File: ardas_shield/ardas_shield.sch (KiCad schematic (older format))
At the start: 37 parts, among them CON1 SD_Card, IC1 DS1307, P1 CONN_10, P10 CONN_01X03, P2 CONN_8, P3 CONN_8, P4 CONN_ICSP, P5 CONN_6, P6 TTL_COMM, P7 CONN_01X03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

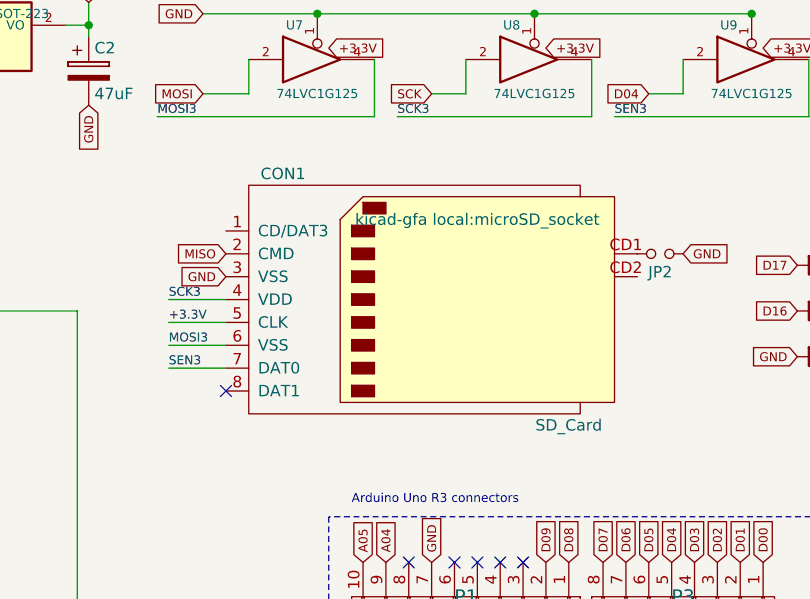
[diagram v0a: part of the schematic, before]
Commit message: removing CON1 SD card
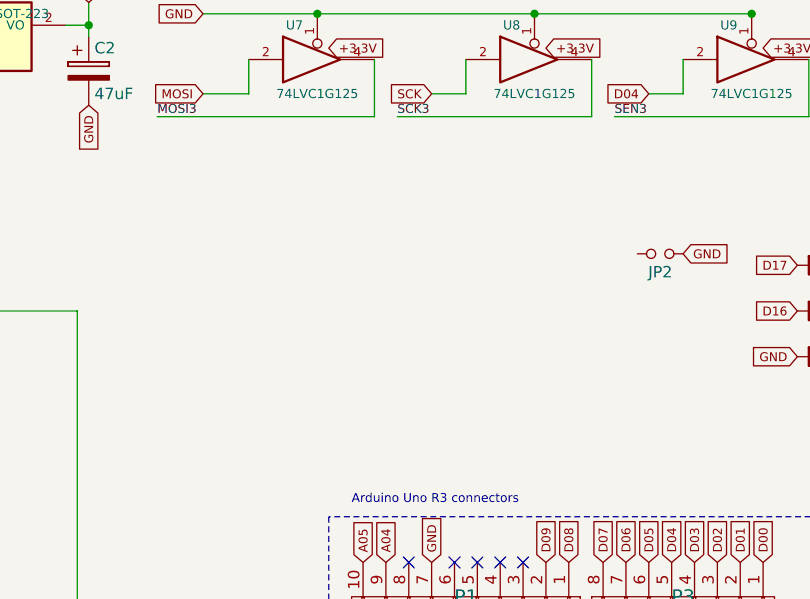
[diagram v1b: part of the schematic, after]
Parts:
- removed CON1: SD_Card, kicad-gfa local:microSD_socket, symbol SD_Card
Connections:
- no-connect marks 20 -> 19
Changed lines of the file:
@@
 Text GLabel 10600 1250 0    39   Input ~ 0
 SCK
-Text GLabel 9700 1950 0    39   Input ~ 0
-MISO
-Text GLabel 9700 2050 0    39   Input ~ 0
-GND
-Text Label 9450 2150 0    39   ~ 0
-SCK3
-Text Label 9450 2250 0    39   ~ 0
-+3.3V
 Text GLabel 8600 1250 3    39   Input ~ 0
 GND
-Text Label 9450 2350 0    39   ~ 0
-MOSI3
-Text Label 9450 2450 0    39   ~ 0
-SEN3
 $Comp
 L CONN_02X03 P4
@@
 Text GLabel 12050 4150 2    39   Input ~ 0
 GND
-NoConn ~ 9700 2550
 Text Notes 12850 3050 0    39   ~ 0
 Rx
@@
 NoConn ~ 2000 4200
 NoConn ~ 13200 1000
-$Comp
-L SD_Card CON1
-U 1 1 5655FE06
-P 10600 2150
-F 0 "CON1" H 9950 2700 50  0000 C CNN
-F 1 "SD_Card" H 11200 1600 50  0000 C CNN
-F 2 "kicad-gfa local:microSD_socket" H 10800 2500 50  0000 C CNN
-F 3 "https://github.com/UMONS-GFA/kicad-gfa.pretty/blob/master/datasheets/1717993.pdf" H 10600 2150 60  0001 C CNN
-F 4 "2334075" H 10600 2150 60  0001 C CNN "Order_Code"
-F 5 "MOLEX" H 10600 2150 60  0001 C CNN "MFN"
-F 6 "503182-1853" H 10600 2150 60  0001 C CNN "MFP"
-	1    10600 2150
-	1    0    0    -1
-$EndComp
 Wire Wire Line
 	5300 1600 5300 2600
@@
 Wire Notes Line
 	12300 5000 12300 3100
-Wire Wire Line
-	9700 2150 9450 2150
-Wire Wire Line
-	9700 2250 9450 2250
 Wire Wire Line
 	11700 1250 11550 1250
@@
 Text GLabel 11700 1950 2    39   Input ~ 0
 GND
-Wire Wire Line
-	9700 2350 9450 2350
-Wire Wire Line
-	9700 2450 9450 2450
 Text GLabel 10150 1050 2    39   Input ~ 0
 +3.3V

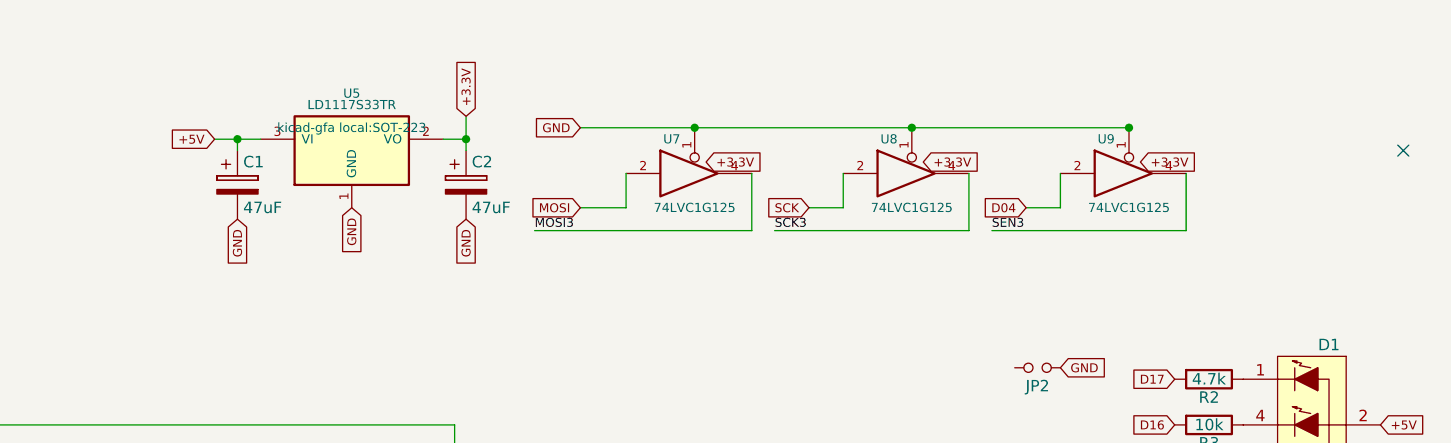
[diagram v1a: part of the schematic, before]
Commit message: removing 5V-3.3V converter components from scheme
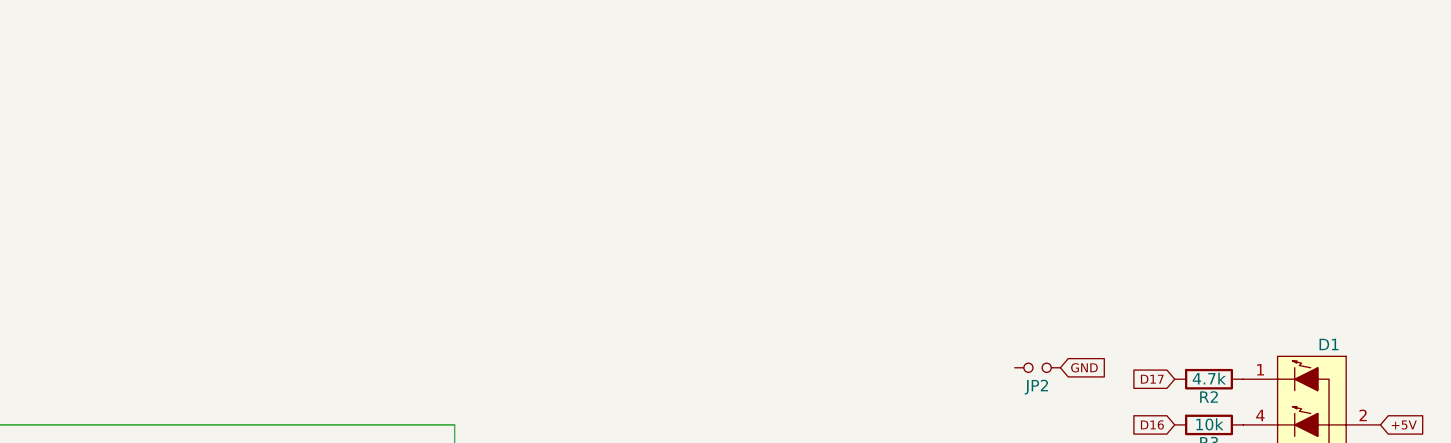
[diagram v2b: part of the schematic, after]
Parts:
- removed C1, C2: 47uF, kicad-gfa local:C_0805, symbol CP
- removed U5: LD1117S33TR, kicad-gfa local:SOT-223, symbol LD1117S33TR
- removed U7, U8, U9: 74LVC1G125, kicad-gfa local:SC-70-5, symbol 74LVC1G125
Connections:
- no-connect marks 19 -> 18
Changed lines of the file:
@@
 	1    0    0    -1
 $EndComp
-Text GLabel 9100 1300 3    39   Input ~ 0
-GND
 Text Notes 10250 3050 0    39   ~ 0
 Arduino Uno R3 connectors
-Text GLabel 8100 1300 3    39   Input ~ 0
-GND
-Text GLabel 9600 900  0    39   Input ~ 0
-GND
-$Comp
-L 74LVC1G125 U7
-U 1 1 56550034
-P 10100 1100
-F 0 "U7" H 10000 1250 40  0000 C CNN
-F 1 "74LVC1G125" H 10100 950 40  0000 C CNN
-F 2 "kicad-gfa local:SC-70-5" H 10100 1100 60  0001 C CNN
-F 3 "" H 10100 1100 60  0000 C CNN
-	1    10100 1100
-	1    0    0    -1
-$EndComp
-$Comp
-L 74LVC1G125 U8
-U 1 1 56550392
-P 11050 1100
-F 0 "U8" H 10950 1250 40  0000 C CNN
-F 1 "74LVC1G125" H 11050 950 40  0000 C CNN
-F 2 "kicad-gfa local:SC-70-5" H 11050 1100 60  0001 C CNN
-F 3 "" H 11050 1100 60  0000 C CNN
-	1    11050 1100
-	1    0    0    -1
-$EndComp
-$Comp
-L 74LVC1G125 U9
-U 1 1 5655048F
-P 12000 1100
-F 0 "U9" H 11900 1250 40  0000 C CNN
-F 1 "74LVC1G125" H 12000 950 40  0000 C CNN
-F 2 "kicad-gfa local:SC-70-5" H 12000 1100 60  0001 C CNN
-F 3 "" H 12000 1100 60  0000 C CNN
-	1    12000 1100
-	1    0    0    -1
-$EndComp
-Text Label 9400 1350 0    39   ~ 0
-MOSI3
-Text Label 10450 1350 0    39   ~ 0
-SCK3
-Text Label 11400 1350 0    39   ~ 0
-SEN3
-Text GLabel 11550 1250 0    39   Input ~ 0
-D04
-$Comp
-L LD1117S33TR U5
-U 1 1 565533AB
-P 8600 1000
-F 0 "U5" H 8600 1250 40  0000 C CNN
-F 1 "LD1117S33TR" H 8600 1200 40  0000 C CNN
-F 2 "kicad-gfa local:SOT-223" H 8600 1100 40  0000 C CNN
-F 3 "https://github.com/UMONS-GFA/kicad-gfa.pretty/blob/master/datasheets/1776449.pdf" H 8600 1000 60  0001 C CNN
-F 4 "1202826" H 8600 1000 60  0001 C CNN "Order_Code"
-F 5 "STMICROELECTRONICS" H 8600 1000 60  0001 C CNN "MFN"
-F 6 " LD1117S33TR" H 8600 1000 60  0001 C CNN "MFP"
-	1    8600 1000
-	1    0    0    -1
-$EndComp
-$Comp
-L CP C1
-U 1 1 565535F2
-P 8100 1150
-F 0 "C1" H 8125 1250 50  0000 L CNN
-F 1 "47uF" H 8125 1050 50  0000 L CNN
-F 2 "kicad-gfa local:C_0805" H 8138 1000 30  0001 C CNN
-F 3 "" H 8100 1150 60  0000 C CNN
-	1    8100 1150
-	1    0    0    -1
-$EndComp
-$Comp
-L CP C2
-U 1 1 565536BD
-P 9100 1150
-F 0 "C2" H 9125 1250 50  0000 L CNN
-F 1 "47uF" H 9125 1050 50  0000 L CNN
-F 2 "kicad-gfa local:C_0805" H 9138 1000 30  0001 C CNN
-F 3 "" H 9100 1150 60  0000 C CNN
-	1    9100 1150
-	1    0    0    -1
-$EndComp
-Text GLabel 8000 950  0    39   Input ~ 0
-+5V
-Text GLabel 9600 1250 0    39   Input ~ 0
-MOSI
-Text GLabel 10600 1250 0    39   Input ~ 0
-SCK
-Text GLabel 8600 1250 3    39   Input ~ 0
-GND
 $Comp
 L CONN_02X03 P4
@@
 	1    0    0    -1
 $EndComp
-Text GLabel 11100 1050 2    39   Input ~ 0
-+3.3V
-Text GLabel 12050 1050 2    39   Input ~ 0
-+3.3V
 $Comp
 L Battery BT1
@@
 NoConn ~ 4600 2100
 NoConn ~ 2000 4200
-NoConn ~ 13200 1000
 Wire Wire Line
 	5300 1600 5300 2600
@@
 Wire Notes Line
 	12300 5000 12300 3100
-Wire Wire Line
-	11700 1250 11550 1250
-Wire Wire Line
-	10750 1250 10600 1250
-Wire Wire Line
-	9800 1250 9600 1250
-Connection ~ 8100 950
-Wire Wire Line
-	8000 950  8200 950
-Wire Wire Line
-	8100 1000 8100 950
-Connection ~ 9100 950
-Wire Wire Line
-	9100 850  9100 1000
-Wire Wire Line
-	9000 950  9100 950
-Wire Wire Line
-	10350 1350 10350 1100
-Wire Wire Line
-	9400 1350 10350 1350
-Wire Wire Line
-	9800 1100 9800 1250
-Wire Wire Line
-	12250 1350 12250 1100
-Wire Wire Line
-	11400 1350 12250 1350
-Wire Wire Line
-	11700 1100 11700 1250
-Wire Wire Line
-	11300 1350 10450 1350
-Wire Wire Line
-	11300 1100 11300 1350
-Wire Wire Line
-	10750 1100 10750 1250
-Connection ~ 11050 900
-Connection ~ 10100 900
 Wire Notes Line
 	10150 3100 10150 5000
@@
 Connection ~ 6950 4300
 Connection ~ 6950 4000
-Connection ~ 12000 900
-Wire Wire Line
-	9600 900  12000 900
 Wire Wire Line
 	6950 4000 6950 4300
@@
 Text GLabel 11700 1950 2    39   Input ~ 0
 GND
-Text GLabel 10150 1050 2    39   Input ~ 0
-+3.3V
-Text GLabel 9100 850  1    39   Input ~ 0
-+3.3V
 Text Notes 9250 6650 0    60   Italic 12
 SHOULDN'T WE SET PIN 10 TO GND OR VCC?

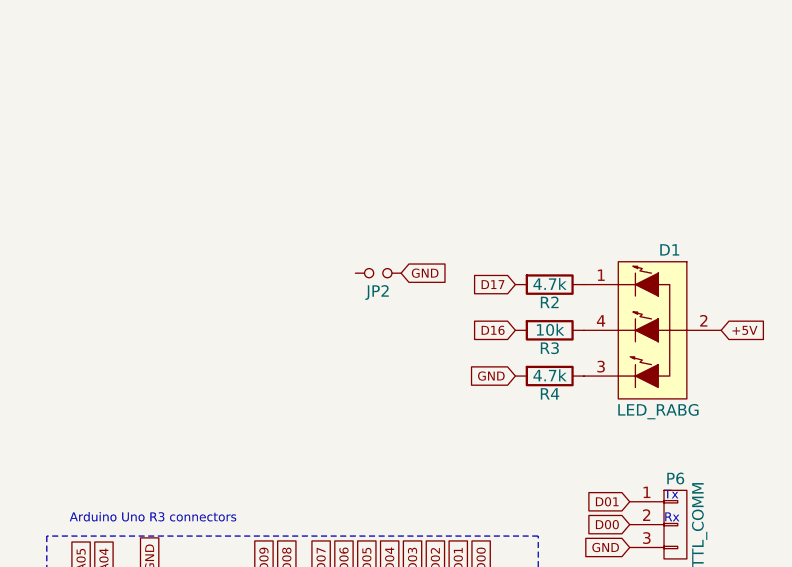
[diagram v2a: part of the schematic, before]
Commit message: removing JP2 from scheme
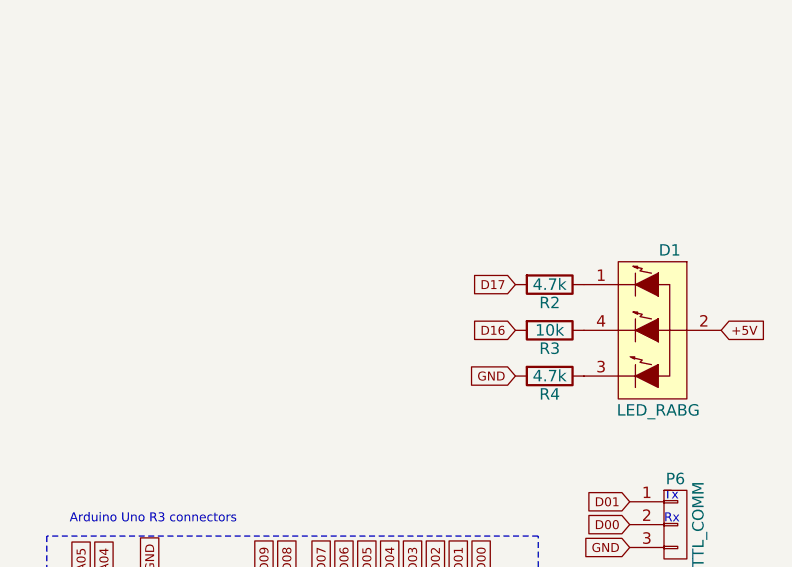
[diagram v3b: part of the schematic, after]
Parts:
- removed JP2: Jumper_NO_Small, kicad-gfa local:small_no_jumper, symbol Jumper_NO_Small
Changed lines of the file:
@@
 NoConn ~ 11950 4800
 NoConn ~ 12050 4800
-$Comp
-L Jumper_NO_Small JP2
-U 1 1 569E9D5A
-P 11600 1950
-F 0 "JP2" H 11600 2030 50  0000 C CNN
-F 1 "Jumper_NO_Small" H 11610 1890 50  0001 C CNN
-F 2 "kicad-gfa local:small_no_jumper" H 11600 1950 50  0001 C CNN
-F 3 "" H 11600 1950 50  0000 C CNN
-	1    11600 1950
-	-1   0    0    1
-$EndComp
-Text GLabel 11700 1950 2    39   Input ~ 0
-GND
 Text Notes 9250 6650 0    60   Italic 12
 SHOULDN'T WE SET PIN 10 TO GND OR VCC?

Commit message: resolve rules check problems
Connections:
- net D04: no longer names the net of P3.5 (P5)
- net MISO: no longer names the net of P4.1 (P1)
- net MOSI: no longer names the net of P4.4 (P4)
- net SCK: no longer names the net of P4.3 (P3)
- no-connect marks 18 -> 22
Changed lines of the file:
@@
 Text GLabel 11750 3300 1    39   Input ~ 0
 D03
-Text GLabel 11650 3300 1    39   Input ~ 0
-D04
 Text GLabel 11550 3300 1    39   Input ~ 0
 D05
@@
 Text GLabel 12050 3950 2    39   Input ~ 0
 +5V
-Text GLabel 11550 3950 0    39   Input ~ 0
-MISO
-Text GLabel 11550 4050 0    39   Input ~ 0
-SCK
-Text GLabel 12050 4050 2    39   Input ~ 0
-MOSI
 Text GLabel 12050 4150 2    39   Input ~ 0
 GND
@@
 Text Notes 9250 6650 0    60   Italic 12
 SHOULDN'T WE SET PIN 10 TO GND OR VCC?
+NoConn ~ 12050 4050
+NoConn ~ 11550 3950
+NoConn ~ 11550 4050
+NoConn ~ 11650 3300
 $EndSCHEMATC

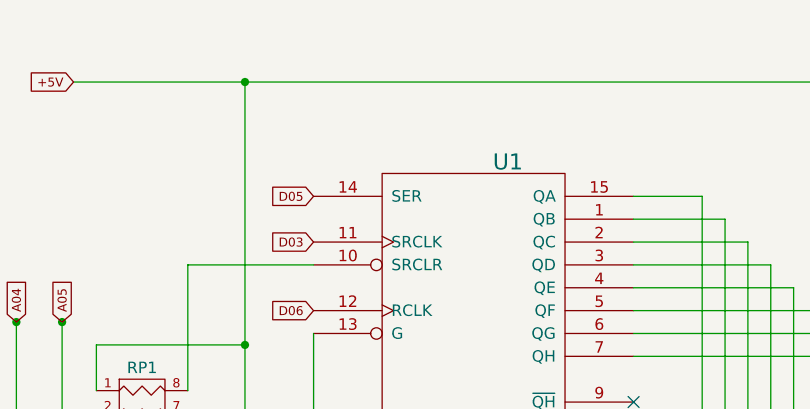
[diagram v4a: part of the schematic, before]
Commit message: resolve power input problem on U1
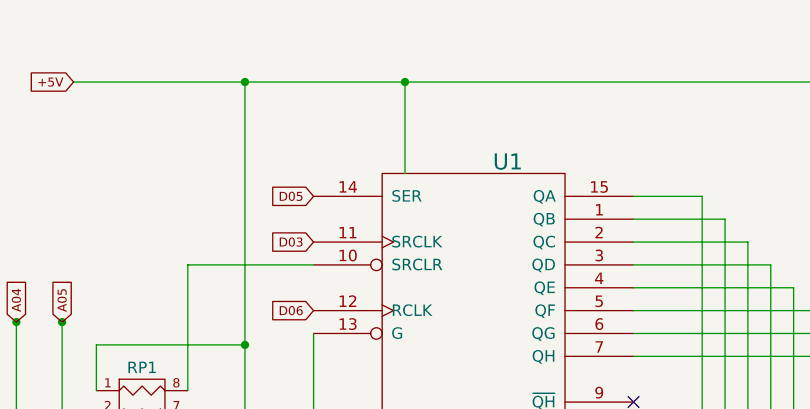
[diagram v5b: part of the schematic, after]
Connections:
- net VCC is gone; now on net +5V: U1.16 (VCC)
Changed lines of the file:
@@
 NoConn ~ 11550 4050
 NoConn ~ 11650 3300
+Wire Wire Line
+	3600 1100 3600 700
+Connection ~ 3600 700
 $EndSCHEMATC

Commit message: replace RGB Led circuit by separated leds
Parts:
- removed D1: LED_RABG, kicad-gfa local:led-P-LCC-4-3, symbol LED_RABG
- added D1, D2, D3: LED, symbol LED
- R2: value 4.7k -> R; footprint kicad-gfa local:R_0805 -> (none); Case_Style 0805 [2012 Metric] -> (none); MFN YAGEO (PHYCOMP) -> (none); MFP RC0805JR-07150RL -> (none); Order_Code 9233903RL -> (none)
- R3: value 10k -> R; footprint kicad-gfa local:R_0805 -> (none); Case_Style 0805 [2012 Metric] -> (none); MFN YAGEO (PHYCOMP) -> (none); MFP RC0805JR-07100RL -> (none); Order_Code 9233881 -> (none)
- R4: value 4.7k -> R; footprint kicad-gfa local:R_0805 -> (none); Case_Style 805 [2012 Metric] -> (none); MFN YAGEO (PHYCOMP) -> (none); MFP RC0805JR-07100RL -> (none); Order_Code 9233881 -> (none)
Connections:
- wire segments 194 -> 202
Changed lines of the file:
@@
 	-1   0    0    1
 $EndComp
-Text GLabel 12200 2200 0    39   Input ~ 0
+Text GLabel 10550 2250 0    39   Input ~ 0
 D16
 Text GLabel 11850 4800 3    39   Input ~ 0
 D17
-Text GLabel 12200 2000 0    39   Input ~ 0
+Text GLabel 10550 1950 0    39   Input ~ 0
 D17
 $Comp
@@
 	1    0    0    -1
 $EndComp
-$Comp
-L LED_RABG D1
-U 1 1 565885AB
-P 12800 2200
-F 0 "D1" H 12875 2550 50  0000 C CNN
-F 1 "LED_RABG" H 12825 1850 50  0000 C CNN
-F 2 "kicad-gfa local:led-P-LCC-4-3" H 12750 2150 50  0001 C CNN
-F 3 "https://github.com/UMONS-GFA/kicad-gfa.pretty/blob/master/datasheets/AV02-4186EN_DS_ASMB-MTB0_2014-09-10.pdf" H 12750 2150 50  0001 C CNN
-	1    12800 2200
-	1    0    0    -1
-$EndComp
-Text GLabel 13100 2200 2    39   Input ~ 0
+Text GLabel 11750 2250 2    39   Input ~ 0
 +5V
 NoConn ~ 10700 3300
-Text GLabel 12200 2400 0    39   Input ~ 0
+Text GLabel 10550 2550 0    39   Input ~ 0
 GND
 $Comp
@@
 Wire Wire Line
 	6500 5800 6500 5950
-$Comp
-L R R2
-U 1 1 568BE18A
-P 12350 2000
-F 0 "R2" V 12430 2000 50  0000 C CNN
-F 1 "4.7k" V 12350 2000 50  0000 C CNN
-F 2 "kicad-gfa local:R_0805" V 12280 2000 50  0001 C CNN
-F 3 "" H 12350 2000 50  0000 C CNN
-F 4 "9233903RL " V 12350 2000 60  0001 C CNN "Order_Code"
-F 5 "YAGEO (PHYCOMP) " V 12350 2000 60  0001 C CNN "MFN"
-F 6 "RC0805JR-07150RL" V 12350 2000 60  0001 C CNN "MFP"
-F 7 "0805 [2012 Metric]" V 12350 2000 60  0001 C CNN "Case_Style"
-	1    12350 2000
-	0    1    1    0
-$EndComp
-$Comp
-L R R3
-U 1 1 568BE39C
-P 12350 2200
-F 0 "R3" V 12430 2200 50  0000 C CNN
-F 1 "10k" V 12350 2200 50  0000 C CNN
-F 2 "kicad-gfa local:R_0805" V 12280 2200 50  0001 C CNN
-F 3 "" H 12350 2200 50  0000 C CNN
-F 4 "9233881" V 12350 2200 60  0001 C CNN "Order_Code"
-F 5 "YAGEO (PHYCOMP) " V 12350 2200 60  0001 C CNN "MFN"
-F 6 "RC0805JR-07100RL" V 12350 2200 60  0001 C CNN "MFP"
-F 7 "0805 [2012 Metric]" V 12350 2200 60  0001 C CNN "Case_Style"
-	1    12350 2200
-	0    1    1    0
-$EndComp
-$Comp
-L R R4
-U 1 1 568BE4E9
-P 12350 2400
-F 0 "R4" V 12430 2400 50  0000 C CNN
-F 1 "4.7k" V 12350 2400 50  0000 C CNN
-F 2 "kicad-gfa local:R_0805" V 12280 2400 50  0001 C CNN
-F 3 "" H 12350 2400 50  0000 C CNN
-F 4 "9233881" V 12350 2400 60  0001 C CNN "Order_Code"
-F 5 "YAGEO (PHYCOMP)" V 12350 2400 60  0001 C CNN "MFN"
-F 6 "RC0805JR-07100RL" V 12350 2400 60  0001 C CNN "MFP"
-F 7 "805 [2012 Metric]" V 12350 2400 60  0001 C CNN "Case_Style"
-	1    12350 2400
-	0    1    1    0
-$EndComp
 $Comp
 L Jumper_NO_Small JP1
@@
 	3600 1100 3600 700
 Connection ~ 3600 700
+$Comp
+L R R2
+U 1 1 5B0E7B52
+P 10800 1950
+F 0 "R2" V 10880 1950 50  0000 C CNN
+F 1 "R" V 10800 1950 50  0000 C CNN
+F 2 "" V 10730 1950 50  0000 C CNN
+F 3 "" H 10800 1950 50  0000 C CNN
+	1    10800 1950
+	0    1    1    0
+$EndComp
+$Comp
+L R R3
+U 1 1 5B0E7BC5
+P 10800 2250
+F 0 "R3" V 10880 2250 50  0000 C CNN
+F 1 "R" V 10800 2250 50  0000 C CNN
+F 2 "" V 10730 2250 50  0000 C CNN
+F 3 "" H 10800 2250 50  0000 C CNN
+	1    10800 2250
+	0    1    1    0
+$EndComp
+$Comp
+L R R4
+U 1 1 5B0E7C5F
+P 10800 2550
+F 0 "R4" V 10880 2550 50  0000 C CNN
+F 1 "R" V 10800 2550 50  0000 C CNN
+F 2 "" V 10730 2550 50  0000 C CNN
+F 3 "" H 10800 2550 50  0000 C CNN
+	1    10800 2550
+	0    1    1    0
+$EndComp
+$Comp
+L LED D1
+U 1 1 5B0E7D8D
+P 11300 1950
+F 0 "D1" H 11300 2050 50  0000 C CNN
+F 1 "LED" H 11300 1850 50  0000 C CNN
+F 2 "" H 11300 1950 50  0000 C CNN
+F 3 "" H 11300 1950 50  0000 C CNN
+	1    11300 1950
+	1    0    0    -1
+$EndComp
+$Comp
+L LED D2
+U 1 1 5B0E7E09
+P 11300 2250
+F 0 "D2" H 11300 2350 50  0000 C CNN
+F 1 "LED" H 11300 2150 50  0000 C CNN
+F 2 "" H 11300 2250 50  0000 C CNN
+F 3 "" H 11300 2250 50  0000 C CNN
+	1    11300 2250
+	1    0    0    -1
+$EndComp
+$Comp
+L LED D3
+U 1 1 5B0E7E8F
+P 11300 2550
+F 0 "D3" H 11300 2650 50  0000 C CNN
+F 1 "LED" H 11300 2450 50  0000 C CNN
+F 2 "" H 11300 2550 50  0000 C CNN
+F 3 "" H 11300 2550 50  0000 C CNN
+	1    11300 2550
+	1    0    0    -1
+$EndComp
+Wire Wire Line
+	10550 1950 10650 1950
+Wire Wire Line
+	10550 2250 10650 2250
+Wire Wire Line
+	10550 2550 10650 2550
+Wire Wire Line
+	10950 1950 11100 1950
+Wire Wire Line
+	10950 2250 11100 2250
+Wire Wire Line
+	10950 2550 11100 2550
+Wire Wire Line
+	11500 1950 11500 2550
+Connection ~ 11500 2250
+Wire Wire Line
+	11500 2250 11750 2250
 $EndSCHEMATC

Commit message: add footprints for new leds and resistors
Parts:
- D1, D2, D3: footprint (none) -> kicad-gfa local:LED-0805
- R2, R3, R4: footprint (none) -> kicad-gfa local:R_0805
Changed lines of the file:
@@
 F 0 "R2" V 10880 1950 50  0000 C CNN
 F 1 "R" V 10800 1950 50  0000 C CNN
-F 2 "" V 10730 1950 50  0000 C CNN
+F 2 "kicad-gfa local:R_0805" V 10730 1950 50  0001 C CNN
 F 3 "" H 10800 1950 50  0000 C CNN
 	1    10800 1950
@@
 F 0 "R3" V 10880 2250 50  0000 C CNN
 F 1 "R" V 10800 2250 50  0000 C CNN
-F 2 "" V 10730 2250 50  0000 C CNN
+F 2 "kicad-gfa local:R_0805" V 10730 2250 50  0001 C CNN
 F 3 "" H 10800 2250 50  0000 C CNN
 	1    10800 2250
@@
 F 0 "R4" V 10880 2550 50  0000 C CNN
 F 1 "R" V 10800 2550 50  0000 C CNN
-F 2 "" V 10730 2550 50  0000 C CNN
+F 2 "kicad-gfa local:R_0805" V 10730 2550 50  0001 C CNN
 F 3 "" H 10800 2550 50  0000 C CNN
 	1    10800 2550
@@
 F 0 "D1" H 11300 2050 50  0000 C CNN
 F 1 "LED" H 11300 1850 50  0000 C CNN
-F 2 "" H 11300 1950 50  0000 C CNN
+F 2 "kicad-gfa local:LED-0805" H 11300 1950 50  0001 C CNN
 F 3 "" H 11300 1950 50  0000 C CNN
 	1    11300 1950
@@
 F 0 "D2" H 11300 2350 50  0000 C CNN
 F 1 "LED" H 11300 2150 50  0000 C CNN
-F 2 "" H 11300 2250 50  0000 C CNN
+F 2 "kicad-gfa local:LED-0805" H 11300 2250 50  0001 C CNN
 F 3 "" H 11300 2250 50  0000 C CNN
 	1    11300 2250
@@
 F 0 "D3" H 11300 2650 50  0000 C CNN
 F 1 "LED" H 11300 2450 50  0000 C CNN
-F 2 "" H 11300 2550 50  0000 C CNN
+F 2 "kicad-gfa local:LED-0805" H 11300 2550 50  0001 C CNN
 F 3 "" H 11300 2550 50  0000 C CNN
 	1    11300 2550
